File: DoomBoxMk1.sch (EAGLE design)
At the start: 14 parts, among them Q1 BC109, SW1 DPDT

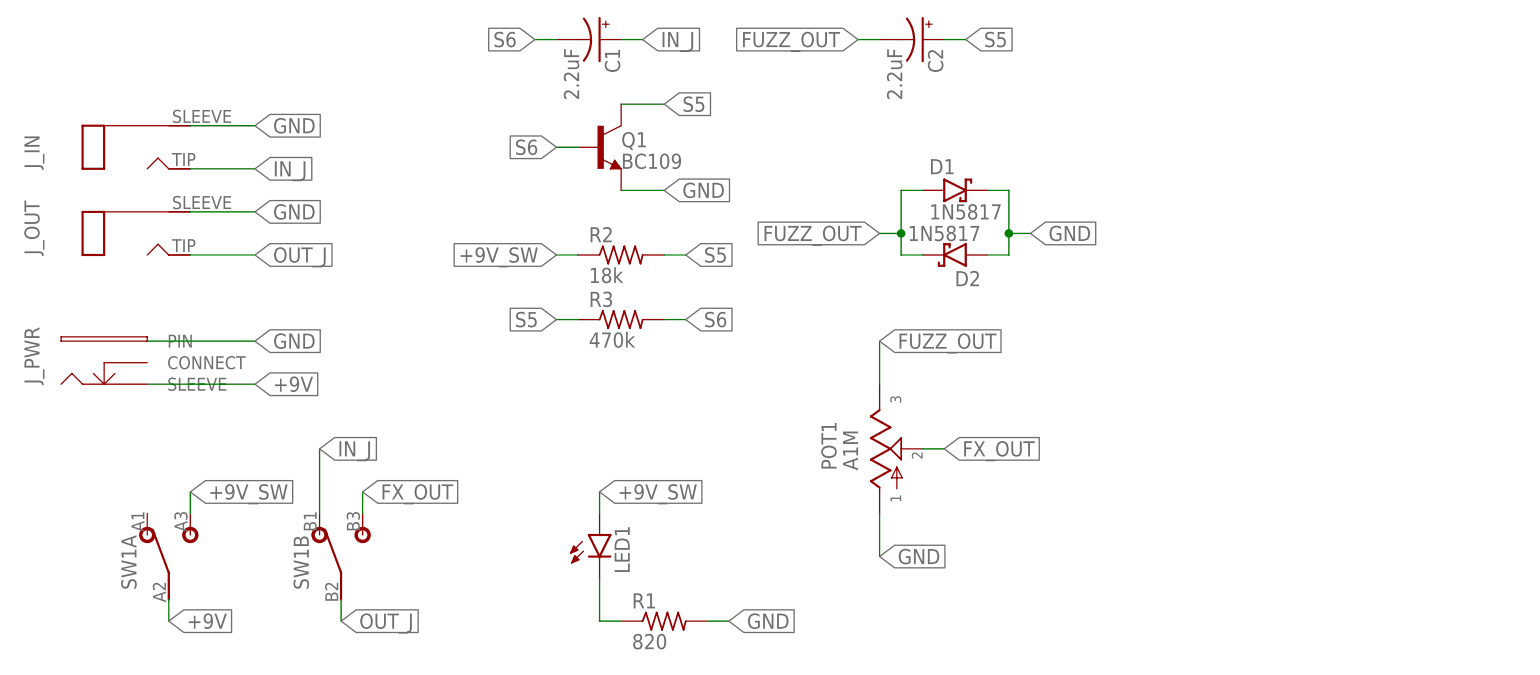
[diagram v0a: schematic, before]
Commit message: Added XR logo and filtered power version
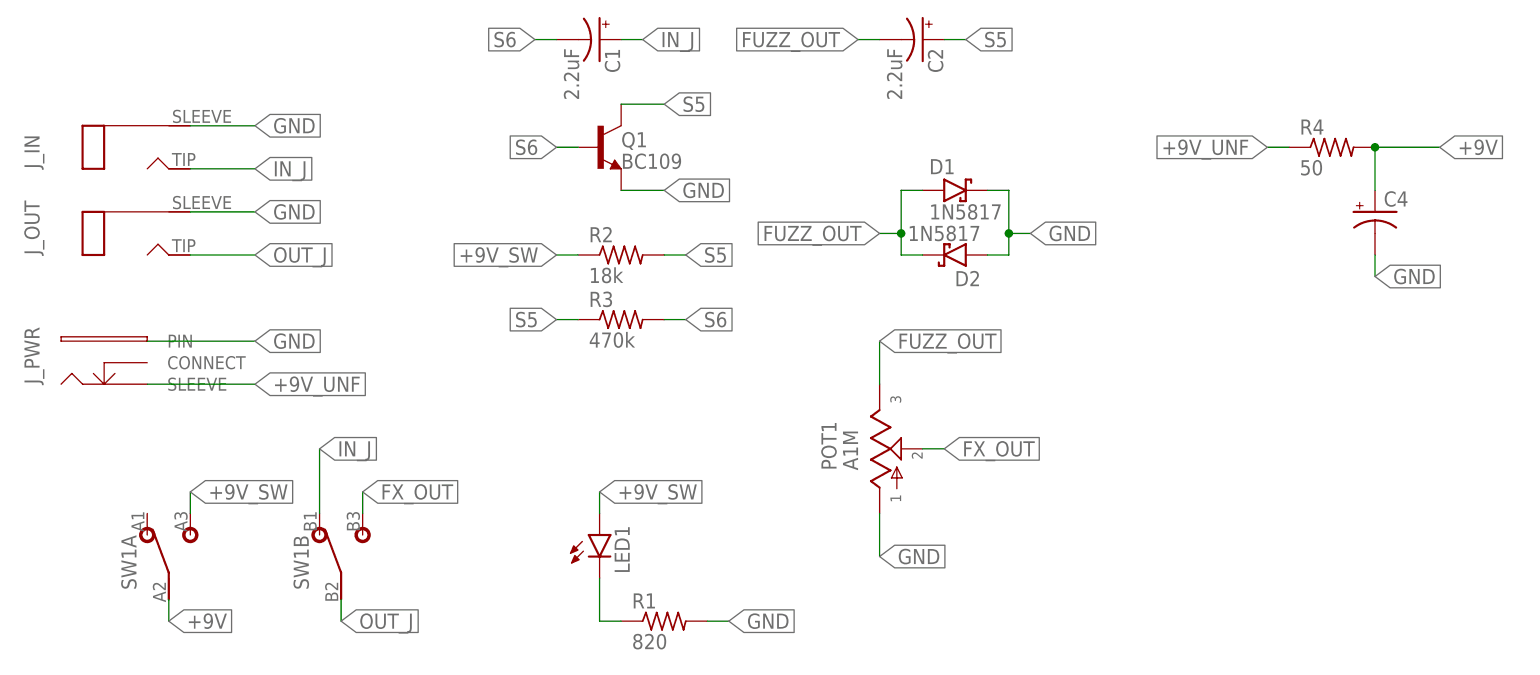
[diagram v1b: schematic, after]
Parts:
- added C4: (no value), gm-caps-electro-pol:0802
- added R4: 50, gm-resistors:6MM.3
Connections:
- new net +9V_UNF: J_PWR.SLEEVE, R4.1
- net +9V: now also C4.+, R4.2; no longer J_PWR.SLEEVE
- net GND: now also C4.-
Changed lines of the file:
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@@
 <part name="C2" library="gm-caps-electro-pol" deviceset="050" device="1" value="2.2uF"/>
 <part name="POT1" library="gm-pots" deviceset="POT" device="S" value="A1M"/>
+<part name="R4" library="gm-resistors" deviceset="6MM" device=".3" value="50"/>
+<part name="C4" library="gm-caps-electro-pol" deviceset="080" device="2"/>
 </parts>
 <sheets>
@@
 <attribute name="VALUE" x="86.36" y="73.66" size="1.778" layer="96" rot="R90"/>
 </instance>
+<instance part="R4" gate="G$1" x="142.24" y="111.76" smashed="yes">
+<attribute name="NAME" x="138.43" y="113.2586" size="1.778" layer="95"/>
+<attribute name="VALUE" x="138.43" y="108.458" size="1.778" layer="96"/>
+</instance>
+<instance part="C4" gate="G$1" x="147.32" y="104.14" smashed="yes">
+<attribute name="NAME" x="148.336" y="104.775" size="1.778" layer="95"/>
+<attribute name="VALUE" x="148.336" y="99.949" size="1.778" layer="96"/>
+</instance>
 </instances>
 <busses>
@@
 <label x="71.12" y="55.88" size="1.778" layer="95" xref="yes"/>
 </segment>
+<segment>
+<wire x1="147.32" y1="99.06" x2="147.32" y2="96.52" width="0.1524" layer="91"/>
+<label x="147.32" y="96.52" size="1.778" layer="95" xref="yes"/>
+<pinref part="C4" gate="G$1" pin="-"/>
+</segment>
 </net>
 <net name="+9V" class="0">
-<segment>
-<wire x1="2.54" y1="83.82" x2="15.24" y2="83.82" width="0.1524" layer="91"/>
-<label x="15.24" y="83.82" size="1.778" layer="95" xref="yes"/>
-<pinref part="J_PWR" gate="G$1" pin="SLEEVE"/>
-</segment>
 <segment>
 <wire x1="5.08" y1="58.42" x2="5.08" y2="55.88" width="0.1524" layer="91"/>
 <label x="5.08" y="55.88" size="1.778" layer="95" xref="yes"/>
 <pinref part="SW1" gate="A" pin="2"/>
+</segment>
+<segment>
+<pinref part="R4" gate="G$1" pin="2"/>
+<wire x1="147.32" y1="111.76" x2="147.32" y2="106.68" width="0.1524" layer="91"/>
+<wire x1="147.32" y1="111.76" x2="154.94" y2="111.76" width="0.1524" layer="91"/>
+<junction x="147.32" y="111.76"/>
+<label x="154.94" y="111.76" size="1.778" layer="95" xref="yes"/>
+<pinref part="C4" gate="G$1" pin="+"/>
 </segment>
 </net>
@@
 </segment>
 </net>
+<net name="+9V_UNF" class="0">
+<segment>
+<pinref part="R4" gate="G$1" pin="1"/>
+<wire x1="137.16" y1="111.76" x2="134.62" y2="111.76" width="0.1524" layer="91"/>
+<label x="134.62" y="111.76" size="1.778" layer="95" rot="R180" xref="yes"/>
+</segment>
+<segment>
+<wire x1="2.54" y1="83.82" x2="15.24" y2="83.82" width="0.1524" layer="91"/>
+<label x="15.24" y="83.82" size="1.778" layer="95" xref="yes"/>
+<pinref part="J_PWR" gate="G$1" pin="SLEEVE"/>
+</segment>
+</net>
